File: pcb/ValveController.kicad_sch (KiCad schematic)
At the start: 87 parts, among them J10 1770966, J11 1770966, J12 1770966, J13 USB4115-03-C, J14 1770966, J15 1770979, J2 1990986, J3 1990986, J8 1770966, J9 1770966, Q3 MOC3063S-TA1, Q4 MOC3063S-TA1, Q5 CSD17313Q2, Q6 CPC1017N, Q7 CPC1017N, SW1 TL9320AF400QG, SW2 TL9320AF400QG, U1 IRM-03-5, U2 TLV75733P, U5 ESP32-C6-WROOM-1-N4, U6 TPS61040, U7 IS31FL3730

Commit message: refactor(pcb): drop SW2 — page button consolidated onto SW1/BOOT
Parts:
- removed SW2: TL9320AF400QG, Kleist2:SW_SPST_TL9320, symbol Switch:SW_Push
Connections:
- net BTN_PAGE: no longer names the net of U5.12 (IO11)
- no-connect marks 11 -> 12
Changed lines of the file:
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@@
 		(at 285.75 213.36)
 	)
+	(no_connect
+		(at 93.98 63.5)
+	)
 	(symbol
 		(lib_id "R_dev")
@@
 	)
 	(symbol
-		(lib_id "Switch:SW_Push")
-		(at 365.76 137.16 0)
-		(unit 1)
-		(body_style 1)
-		(exclude_from_sim no)
-		(in_bom yes)
-		(on_board yes)
-		(in_pos_files yes)
-		(dnp no)
-		(property "Reference" "SW2"
-			(at 368.76 134.16 0)
-			(show_name no)
-			(do_not_autoplace no)
-			(effects
-				(font
-					(size 1.27 1.27)
-				)
-			)
-		)
-		(property "Value" "TL9320AF400QG"
-			(at 368.76 140.16 0)
-			(show_name no)
-			(do_not_autoplace no)
-			(effects
-				(font
-					(size 1.27 1.27)
-				)
-			)
-		)
-		(property "Footprint" "Kleist2:SW_SPST_TL9320"
-			(at 365.76 137.16 0)
-			(show_name no)
-			(do_not_autoplace no)
-			(hide yes)
-			(effects
-				(font
-					(size 1.27 1.27)
-				)
-			)
-		)
-		(property "Datasheet" "https://configured-product-images.s3.amazonaws.com/Datasheets/TL9320.pdf"
-			(at 365.76 137.16 0)
-			(show_name no)
-			(do_not_autoplace no)
-			(hide yes)
-			(effects
-				(font
-					(size 1.27 1.27)
-				)
-			)
-		)
-		(property "Description" "Tactile switch SPST-NO, sealed IP67, matrix page-cycle button"
-			(at 365.76 137.16 0)
-			(show_name no)
-			(do_not_autoplace no)
-			(hide yes)
-			(effects
-				(font
-					(size 1.27 1.27)
-				)
-			)
-		)
-		(property "MPN" "TL9320AF400QG"
-			(at 365.76 137.16 0)
-			(show_name no)
-			(do_not_autoplace no)
-			(hide yes)
-			(effects
-				(font
-					(size 1.27 1.27)
-				)
-			)
-		)
-		(property "DigiKey" "https://www.digikey.com/en/products/detail/e-switch/TL9320AF400QG/11698099"
-			(at 365.76 137.16 0)
-			(show_name no)
-			(do_not_autoplace no)
-			(hide yes)
-			(effects
-				(font
-					(size 1.27 1.27)
-				)
-			)
-		)
-		(pin "1"
-		)
-		(pin "2"
-		)
-		(instances
-			(project "ValveController"
-				(path "/996e7a69-443b-4feb-9505-1512f377356d"
-					(reference "SW2")
-					(unit 1)
-				)
-			)
-		)
-	)
-	(symbol
 		(lib_id "R_dev")
 		(at 375.92 144.78 0)
@@
 		)
 	)
-	(global_label "BTN_PAGE"
-		(shape input)
-		(at 93.98 63.5 180)
-		(effects
-			(font
-				(size 1.27 1.27)
-			)
-			(justify right)
-		)
-		(property "Intersheetrefs" "${INTERSHEET_REFS}"
-			(at 93.98 63.5 0)
-			(hide yes)
-			(show_name no)
-			(do_not_autoplace no)
-			(effects
-				(font
-					(size 1.27 1.27)
-				)
-			)
-		)
-	)
 	(global_label "I2C_SDA"
 		(shape input)
@@
 			(hide yes)
 			(show_name no)
-			(do_not_autoplace no)
-			(effects
-				(font
-					(size 1.27 1.27)
-				)
-			)
-		)
-	)
-	(global_label "BTN_PAGE"
-		(shape input)
-		(at 360.68 137.16 180)
-		(effects
-			(font
-				(size 1.27 1.27)
-			)
-			(justify right)
-		)
-		(property "Intersheetrefs" "${INTERSHEET_REFS}"
-			(at 360.68 137.16 0)
-			(hide yes)
-			(show_name no)
-			(do_not_autoplace no)
-			(effects
-				(font
-					(size 1.27 1.27)
-				)
-			)
-		)
-	)
-	(global_label "GND"
-		(shape input)
-		(at 370.84 137.16 0)
-		(effects
-			(font
-				(size 1.27 1.27)
-			)
-			(justify left)
-		)
-		(property "Intersheetrefs" "${INTERSHEET_REFS}"
-			(at 370.84 137.16 0)
-			(hide yes)
-			(show_name no)

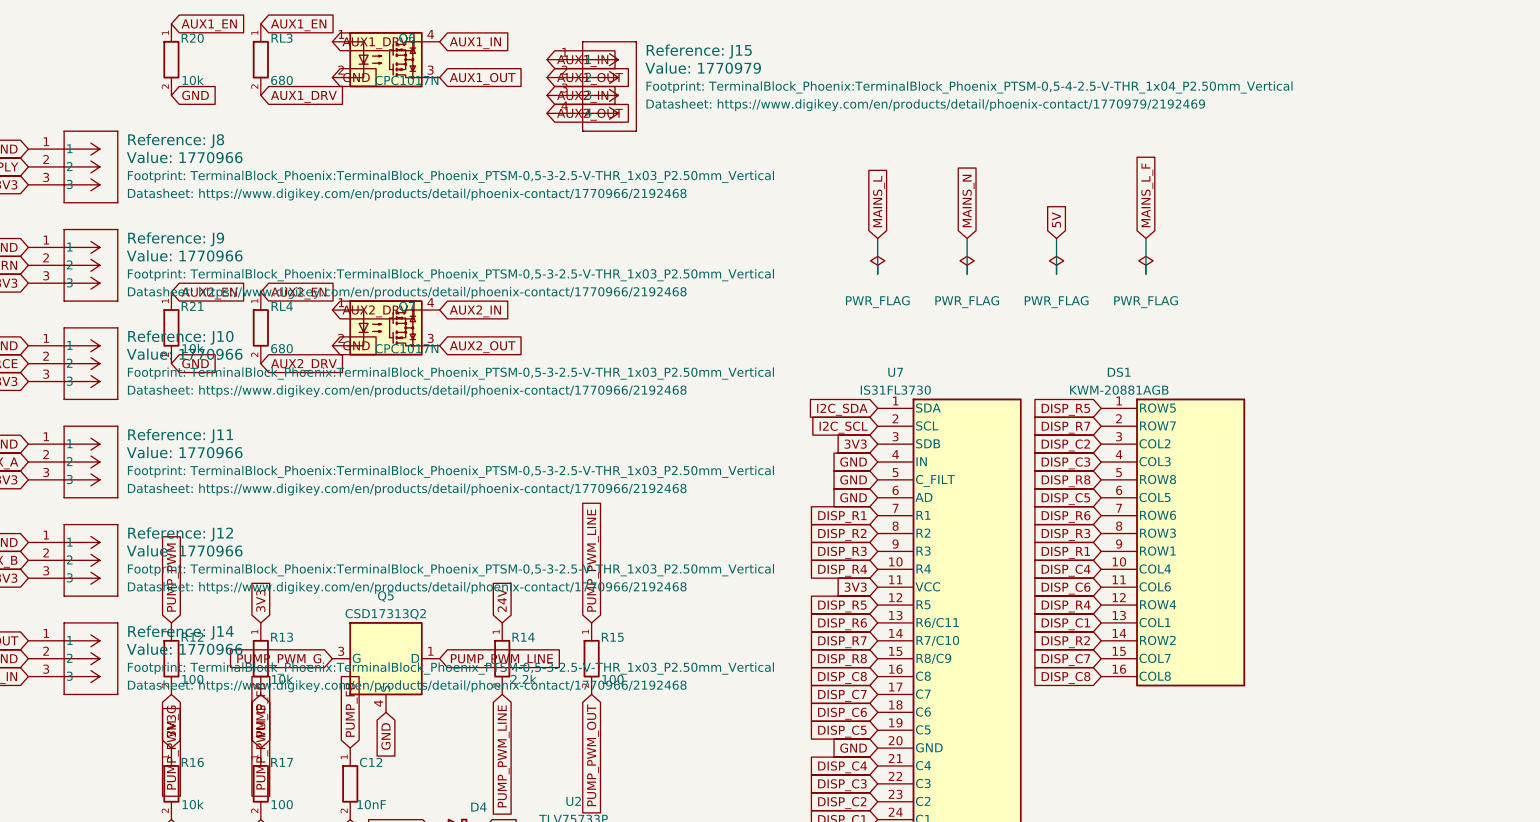
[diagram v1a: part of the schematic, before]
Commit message: feat(pcb): angled PTSM terminals — J14 to 1770898, AUX split into J15+J16 (1770885)
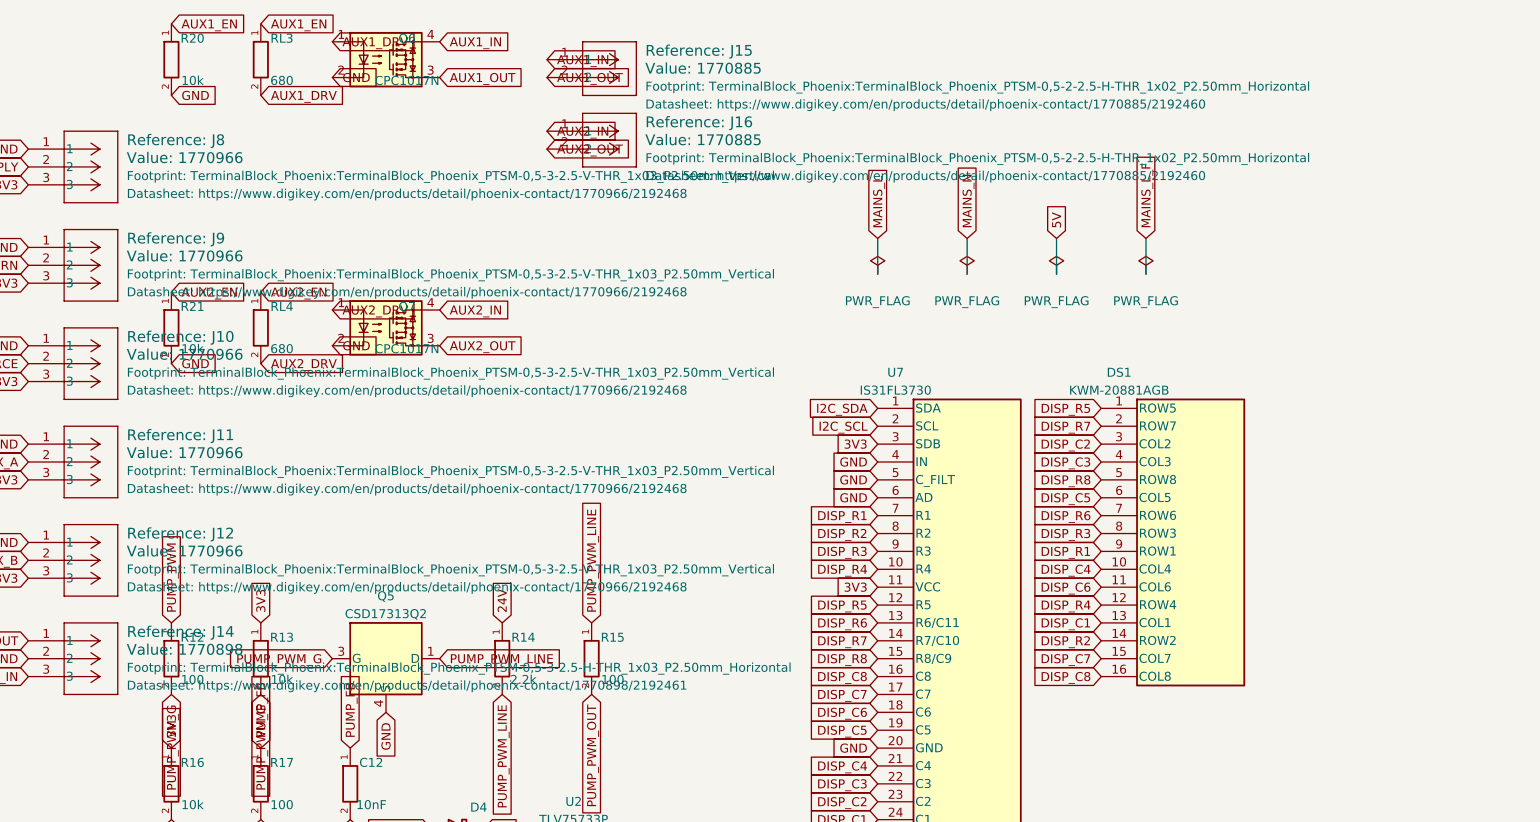
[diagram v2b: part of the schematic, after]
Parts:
- added J16: 1770885, TerminalBlock_Phoenix:TerminalBlock_Phoenix_PTSM-0,5-2-2.5-H-THR_1x02_P2.50mm_Horizontal, symbol Kleist:1770885
- J14: value 1770966 -> 1770898; footprint TerminalBlock_Phoenix:TerminalBlock_Phoenix_PTSM-0,5-3-2.5-V-THR_1x03_P2.50mm_Vertical -> TerminalBlock_Phoenix:TerminalBlock_Phoenix_PTSM-0,5-3-2.5-H-THR_1x03_P2.50mm_Horizontal; DigiKey https://www.digikey.com/en/products/detail/phoenix-contact/1770966/2192468 -> https://www.digikey.com/en/products/detail/phoenix-contact/1770898/2192461; MPN 1770966 -> 1770898
- J15: value 1770979 -> 1770885; footprint TerminalBlock_Phoenix:TerminalBlock_Phoenix_PTSM-0,5-4-2.5-V-THR_1x04_P2.50mm_Vertical -> TerminalBlock_Phoenix:TerminalBlock_Phoenix_PTSM-0,5-2-2.5-H-THR_1x02_P2.50mm_Horizontal; symbol Kleist:1770979 -> Kleist:1770885; DigiKey https://www.digikey.com/en/products/detail/phoenix-contact/1770979/2192469 -> https://www.digikey.com/en/products/detail/phoenix-contact/1770885/2192460; MPN 1770979 -> 1770885
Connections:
- net AUX2_IN: now also J16.1; no longer J15.3
- net AUX2_OUT: now also J16.2; no longer J15.4
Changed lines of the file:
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@@
 			)
 		)
-		(property "Value" "1770966"
+		(property "Value" "1770898"
 			(at 254.0 99.0599 0)
 			(show_name yes)
@@
 			)
 		)
-		(property "Footprint" "TerminalBlock_Phoenix:TerminalBlock_Phoenix_PTSM-0,5-3-2.5-V-THR_1x03_P2.50mm_Vertical"
+		(property "Footprint" "TerminalBlock_Phoenix:TerminalBlock_Phoenix_PTSM-0,5-3-2.5-H-THR_1x03_P2.50mm_Horizontal"
 			(at 254.0 101.5999 0)
 			(show_name yes)
@@
 			)
 		)
-		(property "Datasheet" "https://www.digikey.com/en/products/detail/phoenix-contact/1770966/2192468"
+		(property "Datasheet" "https://www.digikey.com/en/products/detail/phoenix-contact/1770898/2192461"
 			(at 254.0 104.1399 0)
 			(show_name yes)
@@
 			)
 		)
-		(property "MPN" "1770966"
+		(property "MPN" "1770898"
 			(at 240.03 97.79 0)
 			(hide yes)
@@
 			)
 		)
-		(property "DigiKey" "https://www.digikey.com/en/products/detail/phoenix-contact/1770966/2192468"
+		(property "DigiKey" "https://www.digikey.com/en/products/detail/phoenix-contact/1770898/2192461"
 			(at 240.03 97.79 0)
 			(hide yes)
@@
 	)
 	(symbol
-		(lib_id "Kleist:1770979")
+		(lib_id "Kleist:1770885")
 		(at 313.69 15.24 0)
 		(unit 1)
@@
 			)
 		)
-		(property "Value" "1770979"
+		(property "Value" "1770885"
 			(at 327.66 16.51 0)
 			(show_name yes)
@@
 			)
 		)
-		(property "Footprint" "TerminalBlock_Phoenix:TerminalBlock_Phoenix_PTSM-0,5-4-2.5-V-THR_1x04_P2.50mm_Vertical"
+		(property "Footprint" "TerminalBlock_Phoenix:TerminalBlock_Phoenix_PTSM-0,5-2-2.5-H-THR_1x02_P2.50mm_Horizontal"
 			(at 327.66 19.05 0)
 			(show_name yes)
@@
 			)
 		)
-		(property "Datasheet" "https://www.digikey.com/en/products/detail/phoenix-contact/1770979/2192469"
+		(property "Datasheet" "https://www.digikey.com/en/products/detail/phoenix-contact/1770885/2192460"
 			(at 327.66 21.59 0)
 			(show_name yes)
@@
 			)
 		)
-		(property "MPN" "1770979"
+		(property "MPN" "1770885"
 			(at 313.69 15.24 0)
 			(hide yes)
@@
 			)
 		)
-		(property "DigiKey" "https://www.digikey.com/en/products/detail/phoenix-contact/1770979/2192469"
+		(property "DigiKey" "https://www.digikey.com/en/products/detail/phoenix-contact/1770885/2192460"
 			(at 313.69 15.24 0)
 			(hide yes)
@@
 		(pin "2"
 		)
-		(pin "3"
+		(instances
+			(project "ValveController"
+				(path "/996e7a69-443b-4feb-9505-1512f377356d"
+					(reference "J15")
+					(unit 1)
+				)
+			)
 		)
-		(pin "4"
+	)
+	(symbol
+		(lib_id "Kleist:1770885")
+		(at 313.69 25.4 0)
+		(unit 1)
+		(body_style 1)
+		(exclude_from_sim no)
+		(in_bom yes)
+		(on_board yes)
+		(in_pos_files yes)
+		(dnp no)
+		(fields_autoplaced yes)
+		(property "Reference" "J16"
+			(at 327.66 24.13 0)
+			(show_name yes)
+			(do_not_autoplace no)
+			(effects
+				(font
+					(size 1.524 1.524)
+				)
+				(justify left)
+			)
+		)
+		(property "Value" "1770885"
+			(at 327.66 26.67 0)
+			(show_name yes)
+			(do_not_autoplace no)
+			(effects
+				(font
+					(size 1.524 1.524)
+				)
+				(justify left)
+			)
+		)
+		(property "Footprint" "TerminalBlock_Phoenix:TerminalBlock_Phoenix_PTSM-0,5-2-2.5-H-THR_1x02_P2.50mm_Horizontal"
+			(at 327.66 29.21 0)
+			(show_name yes)
+			(do_not_autoplace no)
+			(effects
+				(font
+					(size 1.27 1.27)
+				)
+				(justify left)
+			)
+		)
+		(property "Datasheet" "https://www.digikey.com/en/products/detail/phoenix-contact/1770885/2192460"
+			(at 327.66 31.75 0)
+			(show_name yes)
+			(do_not_autoplace no)
+			(effects
+				(font
+					(size 1.27 1.27)
+				)
+				(justify left)
+			)
+		)
+		(property "Description" ""
+			(at 313.69 25.4 0)
+			(hide yes)
+			(show_name yes)
+			(do_not_autoplace no)
+			(effects
+				(font
+					(size 1.27 1.27)
+				)
+			)
+		)
+		(property "MPN" "1770885"
+			(at 313.69 25.4 0)
+			(hide yes)
+			(show_name no)
+			(do_not_autoplace no)
+			(effects
+				(font
+					(size 1.27 1.27)
+				)
+			)
+		)
+		(property "DigiKey" "https://www.digikey.com/en/products/detail/phoenix-contact/1770885/2192460"
+			(at 313.69 25.4 0)
+			(hide yes)
+			(show_name no)
+			(do_not_autoplace no)
+			(effects
+				(font
+					(size 1.27 1.27)
+				)
+			)
+		)
+		(pin "1"
+		)
+		(pin "2"
 		)
 		(instances
 			(project "ValveController"
 				(path "/996e7a69-443b-4feb-9505-1512f377356d"
-					(reference "J15")
+					(reference "J16")
 					(unit 1)
 				)
@@
 	(global_label "AUX2_IN"
 		(shape input)
-		(at 313.69 20.32 0)
+		(at 313.69 25.4 0)
 		(effects
 			(font
@@
 		)
 		(property "Intersheetrefs" "${INTERSHEET_REFS}"
-			(at 313.69 20.32 0)
+			(at 313.69 25.4 0)
 			(hide yes)
 			(show_name no)
@@
 	(global_label "AUX2_OUT"
 		(shape input)
-		(at 313.69 22.86 0)
+		(at 313.69 27.94 0)
 		(effects
 			(font
@@
 		)
 		(property "Intersheetrefs" "${INTERSHEET_REFS}"
-			(at 313.69 22.86 0)
+			(at 313.69 27.94 0)
 			(hide yes)
 			(show_name no)

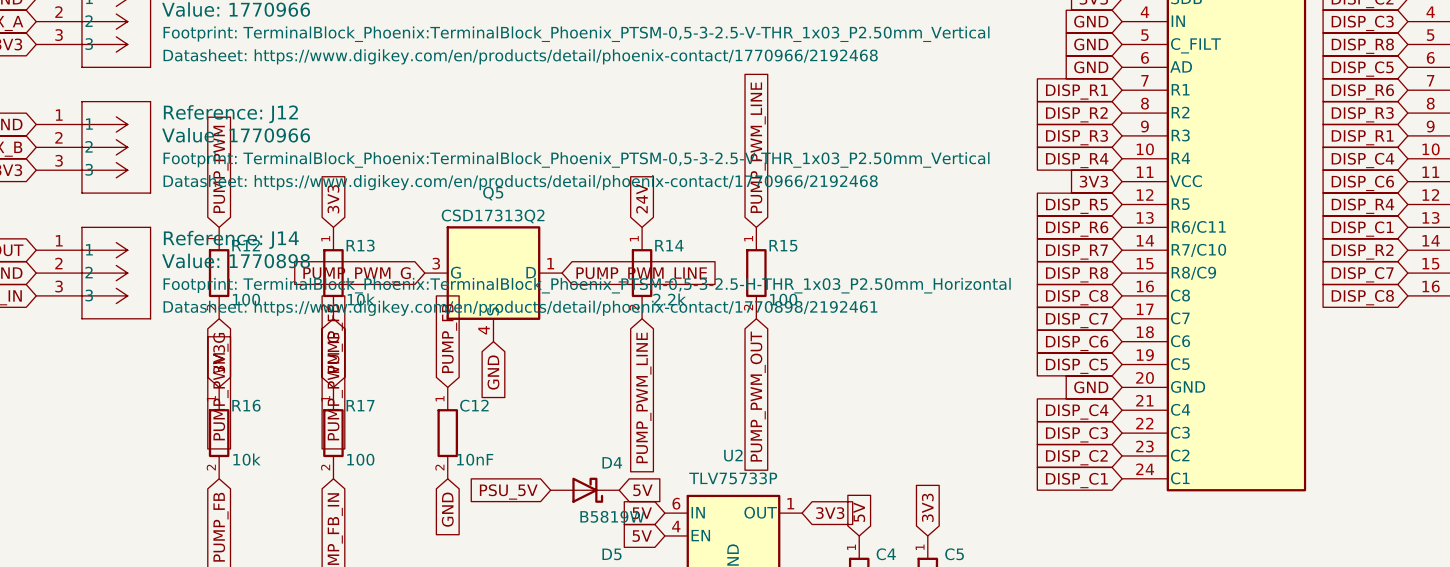
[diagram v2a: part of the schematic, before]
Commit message: fix(pcb): J14 pump terminal to SPT 2,5/3-H-5,0 (1990986), matching J2/J3
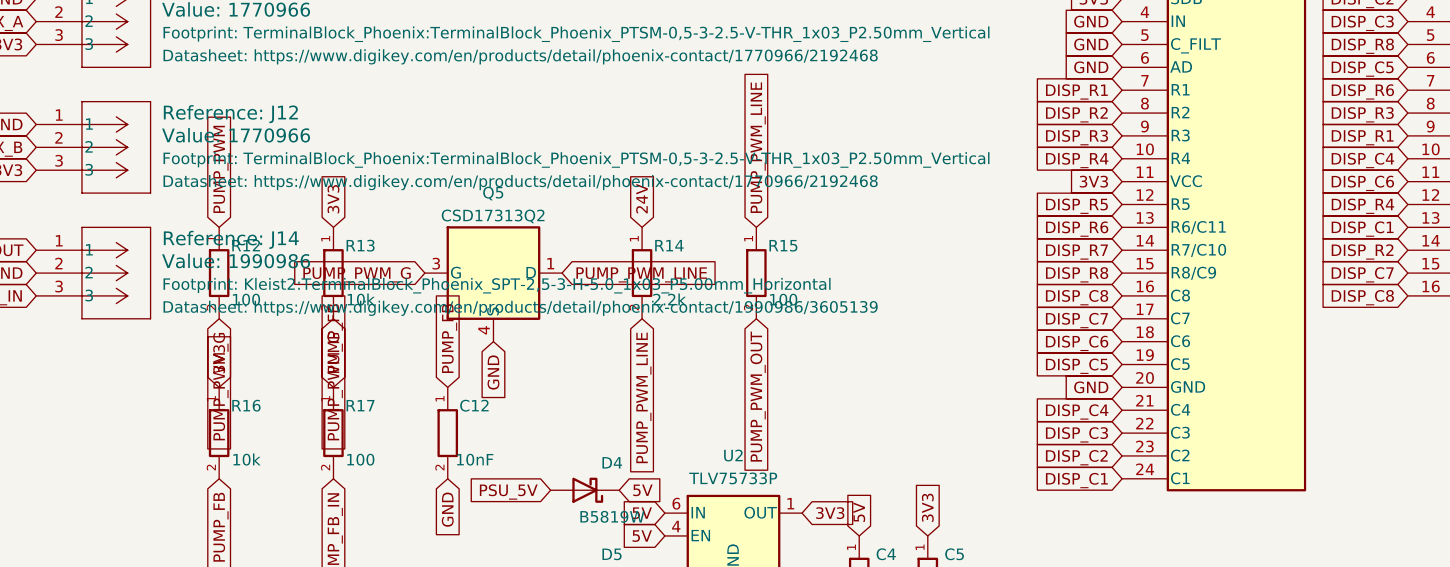
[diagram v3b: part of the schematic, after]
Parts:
- J14: value 1770898 -> 1990986; footprint TerminalBlock_Phoenix:TerminalBlock_Phoenix_PTSM-0,5-3-2.5-H-THR_1x03_P2.50mm_Horizontal -> Kleist2:TerminalBlock_Phoenix_SPT-2,5-3-H-5.0_1x03_P5.00mm_Horizontal; DigiKey https://www.digikey.com/en/products/detail/phoenix-contact/1770898/2192461 -> https://www.digikey.com/en/products/detail/phoenix-contact/1990986/3605139; MPN 1770898 -> 1990986
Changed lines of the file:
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@@
 			)
 		)
-		(property "Value" "1770898"
+		(property "Value" "1990986"
 			(at 254.0 99.0599 0)
 			(show_name yes)
@@
 			)
 		)
-		(property "Footprint" "TerminalBlock_Phoenix:TerminalBlock_Phoenix_PTSM-0,5-3-2.5-H-THR_1x03_P2.50mm_Horizontal"
+		(property "Footprint" "Kleist2:TerminalBlock_Phoenix_SPT-2,5-3-H-5.0_1x03_P5.00mm_Horizontal"
 			(at 254.0 101.5999 0)
 			(show_name yes)
@@
 			)
 		)
-		(property "Datasheet" "https://www.digikey.com/en/products/detail/phoenix-contact/1770898/2192461"
+		(property "Datasheet" "https://www.digikey.com/en/products/detail/phoenix-contact/1990986/3605139"
 			(at 254.0 104.1399 0)
 			(show_name yes)
@@
 			)
 		)
-		(property "MPN" "1770898"
+		(property "MPN" "1990986"
 			(at 240.03 97.79 0)
 			(hide yes)
@@
 			)
 		)
-		(property "DigiKey" "https://www.digikey.com/en/products/detail/phoenix-contact/1770898/2192461"
+		(property "DigiKey" "https://www.digikey.com/en/products/detail/phoenix-contact/1990986/3605139"
 			(at 240.03 97.79 0)
 			(hide yes)
